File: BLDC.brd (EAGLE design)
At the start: 106.7 x 63.5 mm, 56 parts, among them IC1 A4960, Q1 AUIR1324S, Q2 AUIR1324S, Q3 AUIR1324S, Q4 AUIR1324S, Q5 AUIR1324S, Q6 AUIR1324S, U1 MC34063, U2 LM1117-5.0

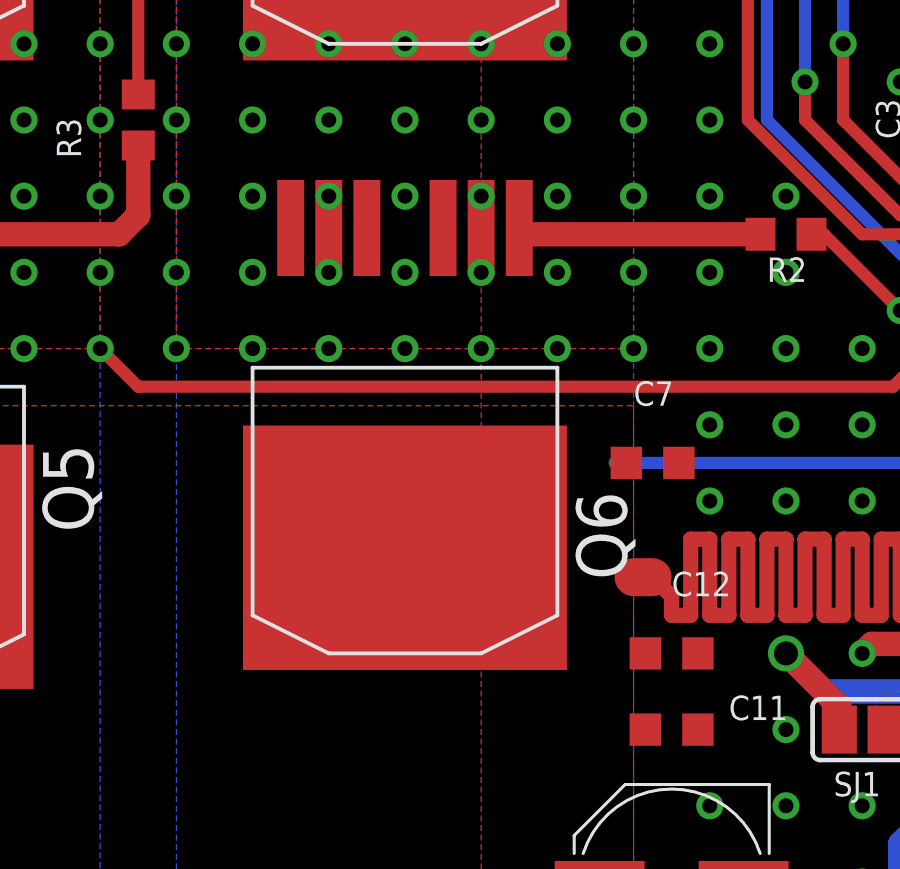
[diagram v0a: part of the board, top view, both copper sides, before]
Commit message: change some values, move R5 to reduce risk of shorting it
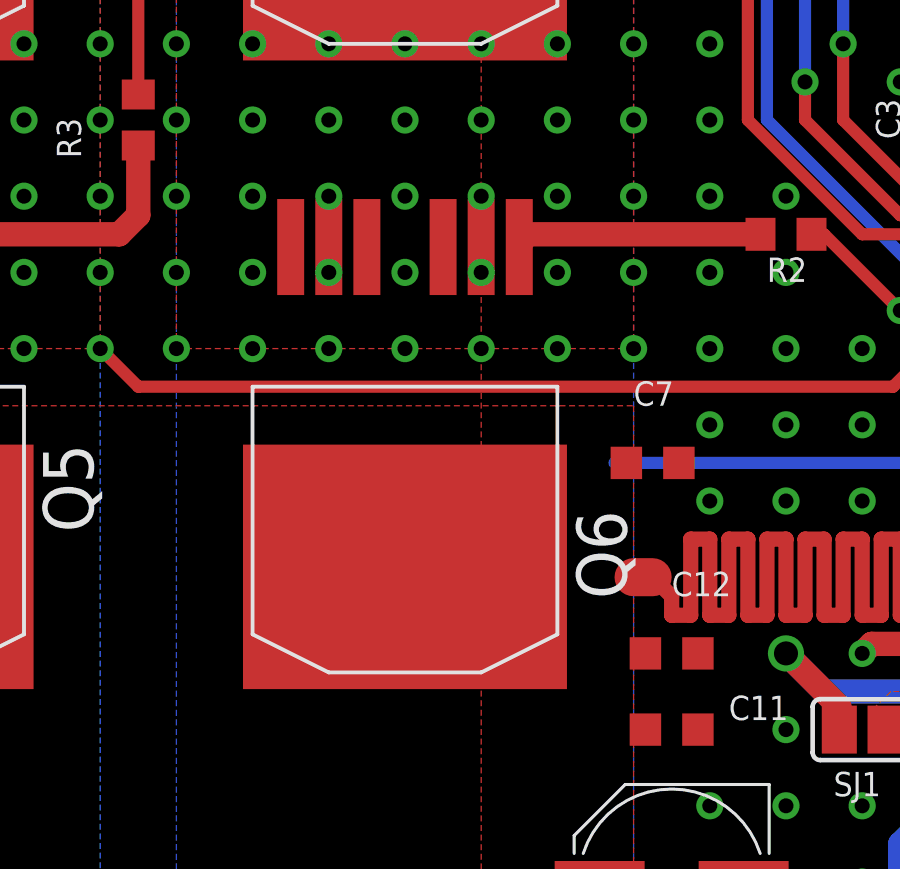
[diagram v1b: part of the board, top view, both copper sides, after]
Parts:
- C1, C2, C3: value 1uF -> 10uF
- C21, C22, C5: value 1uF -> 100nF
- C4: value 1uF -> 220nF
- moved Q6 0.64 mm to (58.4, 27.3)
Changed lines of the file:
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@@
 <wire x1="58.42" y1="13.97" x2="58.42" y2="20.32" width="6.35" layer="29"/>
 <wire x1="40.64" y1="12.7" x2="40.64" y2="19.685" width="6.35" layer="29"/>
+<wire x1="20.32" y1="34.29" x2="20.32" y2="40.64" width="3.81" layer="29"/>
+<wire x1="38.1" y1="40.64" x2="38.1" y2="34.29" width="3.81" layer="29"/>
+<wire x1="55.88" y1="40.64" x2="55.88" y2="34.29" width="3.81" layer="29"/>
+<wire x1="24.765" y1="33.655" x2="24.765" y2="40.64" width="2.1844" layer="29"/>
+<wire x1="42.545" y1="33.655" x2="42.545" y2="40.64" width="2.1844" layer="29"/>
+<wire x1="60.325" y1="33.655" x2="60.325" y2="41.275" width="2.1844" layer="29"/>
+<wire x1="24.765" y1="40.64" x2="24.765" y2="33.655" width="2.1844" layer="31"/>
+<wire x1="42.545" y1="40.64" x2="42.545" y2="33.655" width="2.1844" layer="31"/>
+<wire x1="60.325" y1="33.655" x2="60.325" y2="41.275" width="2.1844" layer="31"/>
+<wire x1="20.32" y1="40.64" x2="20.32" y2="34.29" width="3.81" layer="31"/>
+<wire x1="38.1" y1="34.29" x2="38.1" y2="40.64" width="3.81" layer="31"/>
+<wire x1="55.88" y1="40.64" x2="55.88" y2="34.29" width="3.81" layer="31"/>
 </plain>
 <attributes>
@@
 <attribute name="VALUE" x="82.2325" y="43.815" size="0.8128" layer="27"/>
 </element>
-<element name="C1" library="rcl" package="C0603K" value="1uF" x="86.995" y="30.48" smashed="yes" rot="R135">
+<element name="C1" library="rcl" package="C0603K" value="10uF" x="86.995" y="30.48" smashed="yes" rot="R135">
 <attribute name="NAME" x="85.09" y="29.5275" size="0.8128" layer="25"/>
 <attribute name="VALUE" x="85.09" y="28.575" size="0.8128" layer="27"/>
 </element>
-<element name="C2" library="rcl" package="C0603K" value="1uF" x="78.74" y="32.385" smashed="yes" rot="R180">
+<element name="C2" library="rcl" package="C0603K" value="10uF" x="78.74" y="32.385" smashed="yes" rot="R180">
 <attribute name="NAME" x="76.835" y="34.29" size="0.8128" layer="25"/>
 <attribute name="VALUE" x="76.835" y="33.3375" size="0.8128" layer="27"/>
 </element>
-<element name="C3" library="rcl" package="C0603K" value="1uF" x="76.835" y="38.1" smashed="yes" rot="R90">
+<element name="C3" library="rcl" package="C0603K" value="10uF" x="76.835" y="38.1" smashed="yes" rot="R90">
 <attribute name="NAME" x="74.93" y="37.465" size="0.8128" layer="25" rot="R90"/>
 <attribute name="VALUE" x="75.8825" y="37.465" size="0.8128" layer="27" rot="R90"/>
 </element>
-<element name="C4" library="rcl" package="C0603K" value="1uF" x="90.17" y="33.02" smashed="yes" rot="R315">
+<element name="C4" library="rcl" package="C0603K" value="220nF" x="90.17" y="33.02" smashed="yes" rot="R315">
 <attribute name="NAME" x="92.075" y="32.385" size="0.8128" layer="25"/>
 <attribute name="VALUE" x="92.075" y="31.4325" size="0.8128" layer="27"/>
 </element>
-<element name="C5" library="rcl" package="C0603K" value="1uF" x="89.535" y="30.48" smashed="yes" rot="R315">
+<element name="C5" library="rcl" package="C0603K" value="100nF" x="89.535" y="30.48" smashed="yes" rot="R315">
 <attribute name="NAME" x="91.44" y="29.845" size="0.8128" layer="25"/>
 <attribute name="VALUE" x="91.44" y="28.8925" size="0.8128" layer="27"/>
@@
 <attribute name="VALUE" x="65.405" y="54.61" size="0.8128" layer="27"/>
 </element>
-<element name="C21" library="rcl" package="C0603K" value="1uF" x="89.94549375" y="44.039503125" smashed="yes" rot="R45">
+<element name="C21" library="rcl" package="C0603K" value="100nF" x="89.94549375" y="44.039503125" smashed="yes" rot="R45">
 <attribute name="NAME" x="91.7776875" y="43.615934375" size="0.8128" layer="25" rot="R45"/>
 <attribute name="VALUE" x="92.451534375" y="42.942090625" size="0.8128" layer="27" rot="R45"/>
@@
 <attribute name="VALUE" x="80.01" y="50.165" size="1.27" layer="27"/>
 </element>
-<element name="C22" library="rcl" package="C0603K" value="1uF" x="78.74" y="54.61" smashed="yes" rot="R90">
+<element name="C22" library="rcl" package="C0603K" value="100nF" x="78.74" y="54.61" smashed="yes" rot="R90">
 <attribute name="NAME" x="76.835" y="53.6575" size="0.8128" layer="25" rot="R90"/>
 <attribute name="VALUE" x="77.7875" y="53.6575" size="0.8128" layer="27" rot="R90"/>
@@
 <attribute name="VALUE" x="34.29" y="27.6225" size="1.6764" layer="27" font="vector"/>
 </element>
-<element name="Q6" library="D2PAK-7" package="D2PAK-7" value="AUIR1324S" x="58.42" y="27.94" smashed="yes" rot="R180">
-<attribute name="NAME" x="64.135" y="25.7175" size="1.6764" layer="25" font="vector" rot="R270"/>
-<attribute name="VALUE" x="52.07" y="28.2575" size="1.6764" layer="27" font="vector"/>
+<element name="Q6" library="D2PAK-7" package="D2PAK-7" value="AUIR1324S" x="58.42" y="27.305" smashed="yes" rot="R180">
+<attribute name="NAME" x="64.135" y="25.0825" size="1.6764" layer="25" font="vector" rot="R270"/>
+<attribute name="VALUE" x="52.07" y="27.6225" size="1.6764" layer="27" font="vector"/>
 </element>
 <element name="Q1" library="D2PAK-7" package="D2PAK-7" value="AUIR1324S" x="22.86" y="48.26" smashed="yes" rot="R180">
@@
 <contactref element="R2" pad="2"/>
 <contactref element="Q6" pad="G"/>
-<wire x1="62.44" y1="34.29" x2="62.23" y2="34.5" width="0.8128" layer="1"/>
+<wire x1="62.44" y1="34.29" x2="62.23" y2="33.865" width="0.8128" layer="1"/>
 </signal>
 <signal name="CSM">
